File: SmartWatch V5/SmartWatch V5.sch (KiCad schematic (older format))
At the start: 65 parts, among them J1 10118192-0001LF, J10 TestPad, J11 TestPad, J12 TestPad, J13 TestPad, J14 TestPad, J15 TestPad, J16 TestPad, J17 TestPad, J18 TestPad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

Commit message: Switched LCD_EN with LCD_CS so LCD can remain active using RTC pullup
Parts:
- removed J11, J12, J13, J14: TestPad, CustomFootprints:TESTPAD, symbol CustomParts:TestPad
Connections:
- net LCD_CS: now also U6.27 (IO16); no longer U6.13 (IO14)
- net LCD_LED: now also U6.13 (IO14); no longer U6.27 (IO16)
- no-connect marks 19 -> 23
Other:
- moved on the sheet: C1, C11, R23, U1
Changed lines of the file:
@@
 IO15
-$Comp
-L CustomParts:TestPad J12
-U 1 1 5F244C41
-P 3950 6700
-F 0 "J12" H 4178 6751 50  0000 L CNN
-F 1 "TestPad" H 4178 6660 50  0000 L CNN
-F 2 "CustomFootprints:TESTPAD" H 4050 6800 50  0001 C CNN
-F 3 "" H 4050 6800 50  0001 C CNN
-	1    3950 6700
-	1    0    0    -1
-$EndComp
-$Comp
-L CustomParts:TestPad J11
-U 1 1 5F244C47
-P 3950 6500
-F 0 "J11" H 4178 6551 50  0000 L CNN
-F 1 "TestPad" H 4178 6460 50  0000 L CNN
-F 2 "CustomFootprints:TESTPAD" H 4050 6600 50  0001 C CNN
-F 3 "" H 4050 6600 50  0001 C CNN
-	1    3950 6500
-	1    0    0    -1
-$EndComp
-$Comp
-L CustomParts:TestPad J14
-U 1 1 5F2B6D2C
-P 3950 7100
-F 0 "J14" H 4178 7151 50  0000 L CNN
-F 1 "TestPad" H 4178 7060 50  0000 L CNN
-F 2 "CustomFootprints:TESTPAD" H 4050 7200 50  0001 C CNN
-F 3 "" H 4050 7200 50  0001 C CNN
-	1    3950 7100
-	1    0    0    -1
-$EndComp
-$Comp
-L CustomParts:TestPad J13
-U 1 1 5F2B6D32
-P 3950 6900
-F 0 "J13" H 4178 6951 50  0000 L CNN
-F 1 "TestPad" H 4178 6860 50  0000 L CNN
-F 2 "CustomFootprints:TESTPAD" H 4050 7000 50  0001 C CNN
-F 3 "" H 4050 7000 50  0001 C CNN
-	1    3950 6900
-	1    0    0    -1
-$EndComp
-Wire Wire Line
-	3800 6500 3950 6500
-Wire Wire Line
-	3800 6600 3950 6600
-Wire Wire Line
-	3950 6600 3950 6700
-Wire Wire Line
-	3800 6700 3900 6700
-Wire Wire Line
-	3900 6700 3900 6900
-Wire Wire Line
-	3900 6900 3950 6900
-Wire Wire Line
-	3800 6800 3850 6800
-Wire Wire Line
-	3850 6800 3850 7100
-Wire Wire Line
-	3850 7100 3950 7100
 $Comp
 L CustomParts:TSC2003IPWR U10
@@
 	10100 2450 10300 2450
 Wire Wire Line
+	8050 2550 7600 2550
+Wire Wire Line
+	8050 2750 7600 2750
+Wire Wire Line
+	8050 2950 7600 2950
+Wire Wire Line
+	8050 3150 7600 3150
+Wire Wire Line
 	8050 2350 7600 2350
-Wire Wire Line
-	8050 2750 7600 2750
-Wire Wire Line
-	8050 2950 7600 2950
-Wire Wire Line
-	8050 3150 7600 3150
-Wire Wire Line
-	8050 2550 7600 2550
-Text Label 8050 2350 2    50   ~ 0
+Text Label 8050 2550 2    50   ~ 0
 LCD_CS
 Text Label 8050 2750 2    50   ~ 0
@@
 Text Label 8050 3150 2    50   ~ 0
 LCD_MOSI
-Text Label 8050 2550 2    50   ~ 0
+Text Label 8050 2350 2    50   ~ 0
 LCD_LED
 Text Label 8050 3050 2    50   ~ 0
@@
 Wire Wire Line
 	2250 2550 2350 2550
-Text Label 2250 4100 0    50   ~ 0
+Text Label 2300 3900 0    50   ~ 0
 MAX_REG
 $Comp
 L power:GND #PWR0142
 U 1 1 5EB73B93
-P 1400 4000
-F 0 "#PWR0142" H 1400 3750 50  0001 C CNN
-F 1 "GND" H 1405 3827 50  0000 C CNN
-F 2 "" H 1400 4000 50  0001 C CNN
-F 3 "" H 1400 4000 50  0001 C CNN
-	1    1400 4000
+P 1450 3800
+F 0 "#PWR0142" H 1450 3550 50  0001 C CNN
+F 1 "GND" H 1455 3627 50  0000 C CNN
+F 2 "" H 1450 3800 50  0001 C CNN
+F 3 "" H 1450 3800 50  0001 C CNN
+	1    1450 3800
 	1    0    0    -1
 $EndComp
@@
 L power:GND #PWR02
 U 1 1 5EEB600A
-P 2250 4400
-F 0 "#PWR02" H 2250 4150 50  0001 C CNN
-F 1 "GND" H 2255 4227 50  0000 C CNN
-F 2 "" H 2250 4400 50  0001 C CNN
-F 3 "" H 2250 4400 50  0001 C CNN
-	1    2250 4400
-	1    0    0    -1
-$EndComp
-Wire Wire Line
-	2200 4100 2250 4100
+P 2300 4200
+F 0 "#PWR02" H 2300 3950 50  0001 C CNN
+F 1 "GND" H 2305 4027 50  0000 C CNN
+F 2 "" H 2300 4200 50  0001 C CNN
+F 3 "" H 2300 4200 50  0001 C CNN
+	1    2300 4200
+	1    0    0    -1
+$EndComp
+Wire Wire Line
+	2250 3900 2300 3900
 $Comp
 L Device:C C11
 U 1 1 5EE9CCD7
-P 2250 4250
-F 0 "C11" H 2365 4296 50  0000 L CNN
-F 1 "0.1uF" H 2365 4205 50  0000 L CNN
-F 2 "Capacitor_SMD:C_0603_1608Metric" H 2288 4100 50  0001 C CNN
-F 3 "~" H 2250 4250 50  0001 C CNN
-F 4 "1276-1006-1-ND" H 2250 4250 50  0001 C CNN "digikey"
-	1    2250 4250
+P 2300 4050
+F 0 "C11" H 2415 4096 50  0000 L CNN
+F 1 "0.1uF" H 2415 4005 50  0000 L CNN
+F 2 "Capacitor_SMD:C_0603_1608Metric" H 2338 3900 50  0001 C CNN
+F 3 "~" H 2300 4050 50  0001 C CNN
+F 4 "1276-1006-1-ND" H 2300 4050 50  0001 C CNN "digikey"
+	1    2300 4050
 	1    0    0    -1
 $EndComp
@@
 L power:GND #PWR01
 U 1 1 5EE9C540
-P 1800 4250
-F 0 "#PWR01" H 1800 4000 50  0001 C CNN
-F 1 "GND" H 1800 4100 50  0000 C CNN
-F 2 "" H 1800 4250 50  0001 C CNN
-F 3 "" H 1800 4250 50  0001 C CNN
-	1    1800 4250
-	1    0    0    -1
-$EndComp
-Wire Wire Line
-	2200 3950 2650 3950
-Wire Wire Line
-	2200 3850 2650 3850
-Text Label 2650 3950 2    50   ~ 0
+P 1850 4050
+F 0 "#PWR01" H 1850 3800 50  0001 C CNN
+F 1 "GND" H 1850 3900 50  0000 C CNN
+F 2 "" H 1850 4050 50  0001 C CNN
+F 3 "" H 1850 4050 50  0001 C CNN
+	1    1850 4050
+	1    0    0    -1
+$EndComp
+Wire Wire Line
+	2250 3750 2700 3750
+Wire Wire Line
+	2250 3650 2700 3650
+Text Label 2700 3750 2    50   ~ 0
 I2C_SCL
-Text Label 2650 3850 2    50   ~ 0
+Text Label 2700 3650 2    50   ~ 0
 I2C_SDA
 Wire Wire Line
-	2200 3750 2650 3750
-Text Label 2650 3750 2    50   ~ 0
+	2250 3550 2700 3550
+Text Label 2700 3550 2    50   ~ 0
 BAT_ALRT
 Wire Wire Line
-	2050 3300 2650 3300
-Text Label 2650 3300 2    50   ~ 0
+	2100 3100 2700 3100
+Text Label 2700 3100 2    50   ~ 0
 BAT_SENSE
-Connection ~ 2050 3300
-Wire Wire Line
-	2050 3300 2050 3350
-Wire Wire Line
-	1950 3300 2050 3300
-Connection ~ 1600 3300
-Wire Wire Line
-	900  3300 900  3800
-Wire Wire Line
-	1600 3300 900  3300
-Wire Wire Line
-	1600 3300 1650 3300
-Wire Wire Line
-	1600 3350 1600 3300
+Connection ~ 2100 3100
+Wire Wire Line
+	2100 3100 2100 3150
+Wire Wire Line
+	2000 3100 2100 3100
+Connection ~ 1650 3100
+Wire Wire Line
+	950  3100 950  3600
+Wire Wire Line
+	1650 3100 950  3100
+Wire Wire Line
+	1650 3100 1700 3100
+Wire Wire Line
+	1650 3150 1650 3100
 $Comp
 L Device:R R23
 U 1 1 5EBB9EAC
-P 1800 3300
-F 0 "R23" H 1870 3346 50  0000 L CNN
-F 1 "10m" H 1870 3255 50  0000 L CNN
-F 2 "Resistor_SMD:R_0805_2012Metric" V 1730 3300 50  0001 C CNN
-F 3 "https://d1d2qsbl8m0m72.cloudfront.net/en/products/databook/datasheet/passive/resistor/chip_resistor/pmr-e.pdf" H 1800 3300 50  0001 C CNN
-F 4 "RL12T.010JCT-ND" H 1800 3300 50  0001 C CNN "digikey"
-	1    1800 3300
+P 1850 3100
+F 0 "R23" H 1920 3146 50  0000 L CNN
+F 1 "10m" H 1920 3055 50  0000 L CNN
+F 2 "Resistor_SMD:R_0805_2012Metric" V 1780 3100 50  0001 C CNN
+F 3 "https://d1d2qsbl8m0m72.cloudfront.net/en/products/databook/datasheet/passive/resistor/chip_resistor/pmr-e.pdf" H 1850 3100 50  0001 C CNN
+F 4 "RL12T.010JCT-ND" H 1850 3100 50  0001 C CNN "digikey"
+	1    1850 3100
 	0    -1   -1   0
 $EndComp
 Wire Wire Line
-	1350 3800 1400 3800
-Connection ~ 1350 3800
-Wire Wire Line
-	1350 3900 1350 3800
-Wire Wire Line
-	1400 3900 1350 3900
-Wire Wire Line
-	900  3800 1350 3800
+	1400 3600 1450 3600
+Connection ~ 1400 3600
+Wire Wire Line
+	1400 3700 1400 3600
+Wire Wire Line
+	1450 3700 1400 3700
+Wire Wire Line
+	950  3600 1400 3600
 $Comp
 L Device:C C1
 U 1 1 5E856FED
-P 900 3950
-F 0 "C1" H 600 4000 50  0000 L CNN
-F 1 "10uF" H 600 3900 50  0000 L CNN
-F 2 "Capacitor_SMD:C_0603_1608Metric" H 938 3800 50  0001 C CNN
-F 3 "~" H 900 3950 50  0001 C CNN
-F 4 "478-10766-1-ND" H 900 3950 50  0001 C CNN "digikey"
-	1    900  3950
-	1    0    0    -1
-$EndComp
-Text Label 700  3800 0    50   ~ 0
+P 950 3750
+F 0 "C1" H 650 3800 50  0000 L CNN
+F 1 "10uF" H 650 3700 50  0000 L CNN
+F 2 "Capacitor_SMD:C_0603_1608Metric" H 988 3600 50  0001 C CNN
+F 3 "~" H 950 3750 50  0001 C CNN
+F 4 "478-10766-1-ND" H 950 3750 50  0001 C CNN "digikey"
+	1    950  3750
+	1    0    0    -1
+$EndComp
+Text Label 750  3600 0    50   ~ 0
 BAT+
 Wire Wire Line
-	700  3800 900  3800
-Connection ~ 900  3800
+	750  3600 950  3600
+Connection ~ 950  3600
 $Comp
 L power:GND #PWR0143
 U 1 1 5E91C7C2
-P 900 4100
-F 0 "#PWR0143" H 900 3850 50  0001 C CNN
-F 1 "GND" H 905 3927 50  0000 C CNN
-F 2 "" H 900 4100 50  0001 C CNN
-F 3 "" H 900 4100 50  0001 C CNN
-	1    900  4100
+P 950 3900
+F 0 "#PWR0143" H 950 3650 50  0001 C CNN
+F 1 "GND" H 955 3727 50  0000 C CNN
+F 2 "" H 950 3900 50  0001 C CNN
+F 3 "" H 950 3900 50  0001 C CNN
+	1    950  3900
 	1    0    0    -1
 $EndComp
@@
 L CustomParts:MAX17260 U1
 U 1 1 5F23D031
-P 1800 3850
-F 0 "U1" H 1250 4550 50  0000 C CNN
-F 1 "MAX17260" H 1400 4450 50  0000 C CNN
-F 2 "CustomFootprints:TDFN16-EP" H 1150 5000 50  0001 C CNN
-F 3 "https://datasheets.maximintegrated.com/en/ds/MAX17260.pdf" H 1150 5000 50  0001 C CNN
-F 4 "175-MAX17260SEWL+TCT-ND" H 850 4900 50  0001 C CNN "digikey"
-	1    1800 3850
+P 1850 3650
+F 0 "U1" H 1300 4350 50  0000 C CNN
+F 1 "MAX17260" H 1450 4250 50  0000 C CNN
+F 2 "CustomFootprints:TDFN16-EP" H 1200 4800 50  0001 C CNN
+F 3 "https://datasheets.maximintegrated.com/en/ds/MAX17260.pdf" H 1200 4800 50  0001 C CNN
+F 4 "175-MAX17260SEWL+TCT-ND" H 900 4700 50  0001 C CNN "digikey"
+	1    1850 3650
 	1    0    0    -1
 $EndComp
@@
 Wire Bus Line
 	3150 3250 5900 3250
-Text Notes 3500 2950 0    50   ~ 0
+Text Notes 3500 3000 0    50   ~ 0
 Charging Current of 100mA\n
 Wire Bus Line
@@
 Wire Bus Line
 	6050 5950 6050 6500
+NoConn ~ 3800 6500
+NoConn ~ 3800 6600
+NoConn ~ 3800 6700
+NoConn ~ 3800 6800
 $EndSCHEMATC

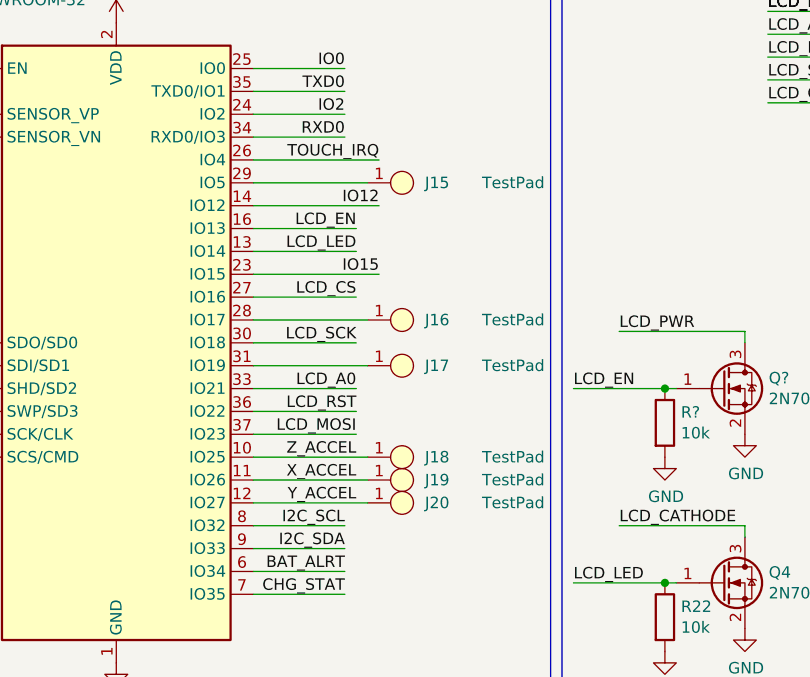
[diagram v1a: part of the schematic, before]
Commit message: Removed testpads that are no longer needed
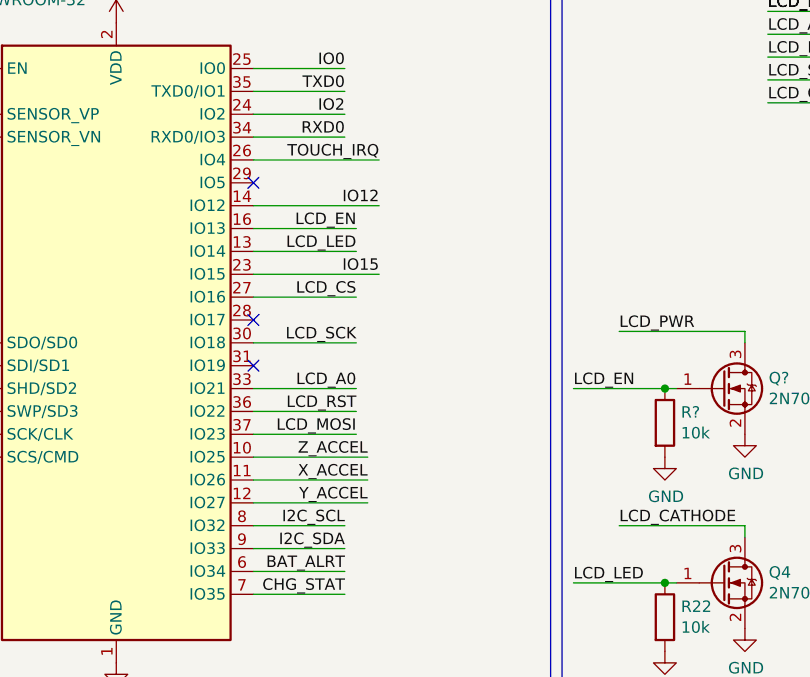
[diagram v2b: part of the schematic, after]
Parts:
- removed J15, J16, J17, J18, J19, J20: TestPad, CustomFootprints:TESTPAD, symbol CustomParts:TestPad
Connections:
- no-connect marks 23 -> 26
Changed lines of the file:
@@
 Text Label 9850 1700 0    50   ~ 0
 LCD_CS
-$Comp
-L CustomParts:TestPad J15
-U 1 1 5F1F3B31
-P 8100 2050
-F 0 "J15" H 8350 2050 50  0000 L CNN
-F 1 "TestPad" H 8600 2050 50  0000 L CNN
-F 2 "CustomFootprints:TESTPAD" H 8200 2150 50  0001 C CNN
-F 3 "" H 8200 2150 50  0001 C CNN
-	1    8100 2050
-	1    0    0    -1
-$EndComp
-$Comp
-L CustomParts:TestPad J16
-U 1 1 5F1F47AF
-P 8100 2650
-F 0 "J16" H 8350 2650 50  0000 L CNN
-F 1 "TestPad" H 8600 2650 50  0000 L CNN
-F 2 "CustomFootprints:TESTPAD" H 8200 2750 50  0001 C CNN
-F 3 "" H 8200 2750 50  0001 C CNN
-	1    8100 2650
-	1    0    0    -1
-$EndComp
-$Comp
-L CustomParts:TestPad J17
-U 1 1 5F1F4D94
-P 8100 2850
-F 0 "J17" H 8350 2850 50  0000 L CNN
-F 1 "TestPad" H 8600 2850 50  0000 L CNN
-F 2 "CustomFootprints:TESTPAD" H 8200 2950 50  0001 C CNN
-F 3 "" H 8200 2950 50  0001 C CNN
-	1    8100 2850
-	1    0    0    -1
-$EndComp
-$Comp
-L CustomParts:TestPad J18
-U 1 1 5F1F51C0
-P 8100 3250
-F 0 "J18" H 8350 3250 50  0000 L CNN
-F 1 "TestPad" H 8600 3250 50  0000 L CNN
-F 2 "CustomFootprints:TESTPAD" H 8200 3350 50  0001 C CNN
-F 3 "" H 8200 3350 50  0001 C CNN
-	1    8100 3250
-	1    0    0    -1
-$EndComp
-$Comp
-L CustomParts:TestPad J19
-U 1 1 5F1F5439
-P 8100 3350
-F 0 "J19" H 8350 3350 50  0000 L CNN
-F 1 "TestPad" H 8600 3350 50  0000 L CNN
-F 2 "CustomFootprints:TESTPAD" H 8200 3450 50  0001 C CNN
-F 3 "" H 8200 3450 50  0001 C CNN
-	1    8100 3350
-	1    0    0    -1
-$EndComp
-$Comp
-L CustomParts:TestPad J20
-U 1 1 5F1F569A
-P 8100 3450
-F 0 "J20" H 8350 3450 50  0000 L CNN
-F 1 "TestPad" H 8600 3450 50  0000 L CNN
-F 2 "CustomFootprints:TESTPAD" H 8200 3550 50  0001 C CNN
-F 3 "" H 8200 3550 50  0001 C CNN
-	1    8100 3450
-	1    0    0    -1
-$EndComp
-Wire Wire Line
-	7600 2050 8100 2050
-Wire Wire Line
-	7600 2650 8100 2650
-Wire Wire Line
-	7600 2850 8100 2850
 Wire Wire Line
 	7600 3250 8100 3250
@@
 Wire Bus Line
 	5900 4650 5900 3300
-Text Label 8050 3250 2    50   ~ 0
+Text Label 8100 3250 2    50   ~ 0
 Z_ACCEL
-Text Label 8050 3350 2    50   ~ 0
+Text Label 8100 3350 2    50   ~ 0
 X_ACCEL
-Text Label 8050 3450 2    50   ~ 0
+Text Label 8100 3450 2    50   ~ 0
 Y_ACCEL
 Text Label 4200 2350 2    50   ~ 0
@@
 NoConn ~ 3800 6700
 NoConn ~ 3800 6800
+NoConn ~ 7600 2050
+NoConn ~ 7600 2650
+NoConn ~ 7600 2850
 $EndSCHEMATC

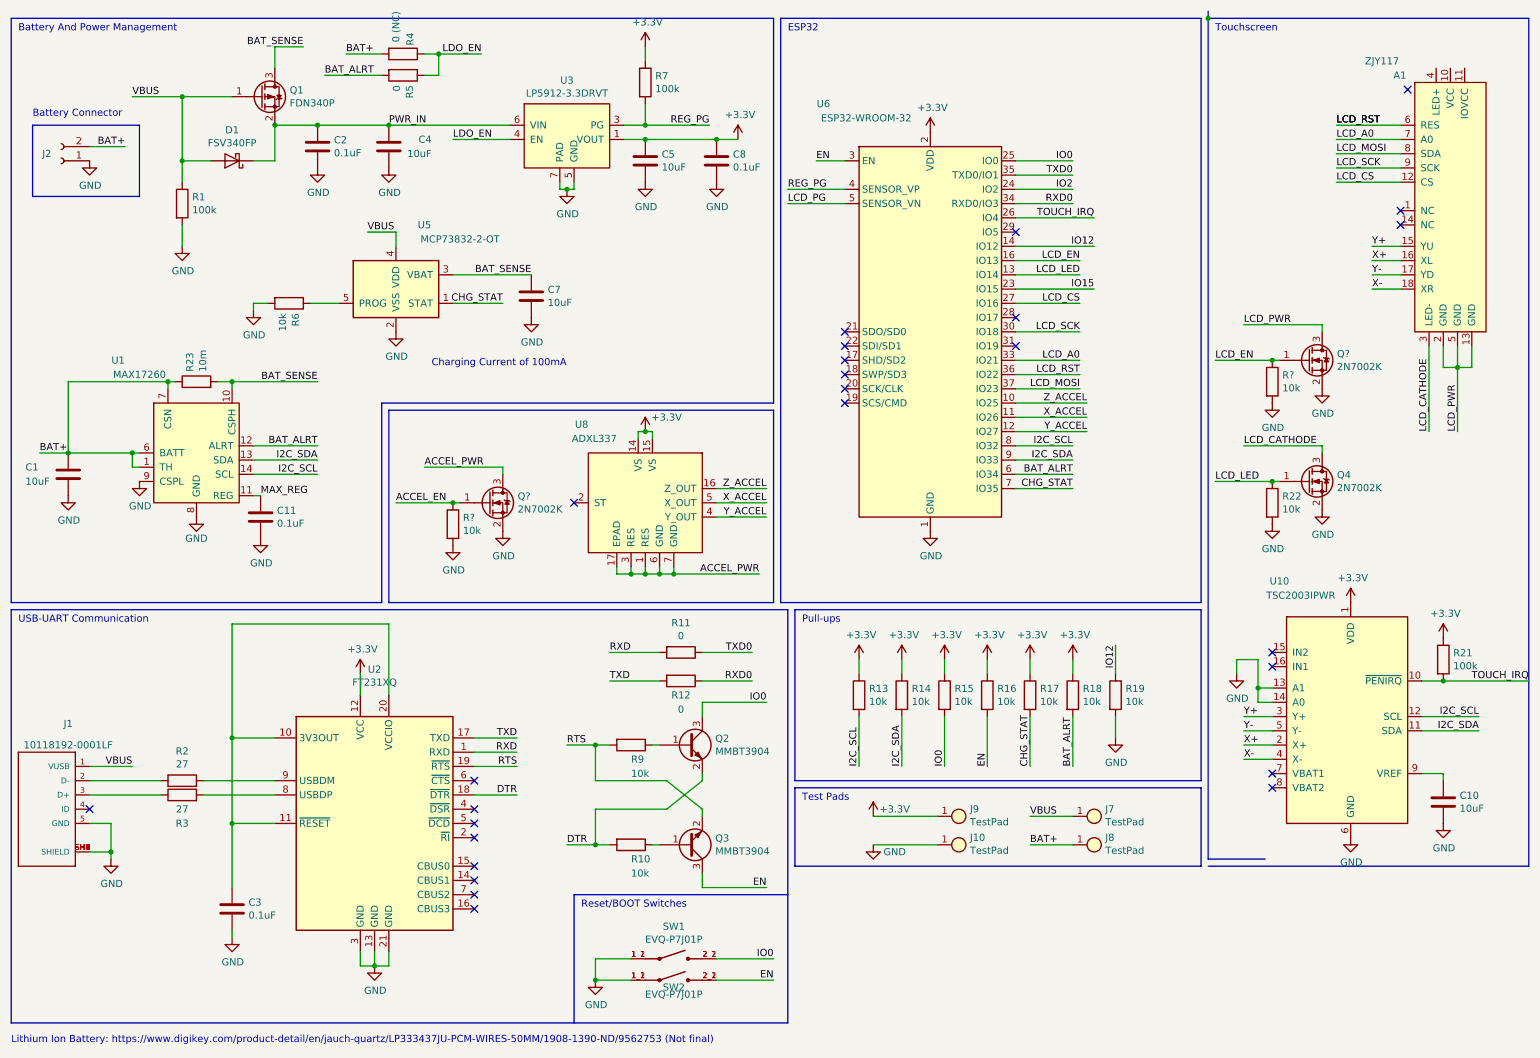
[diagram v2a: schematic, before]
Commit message: Added Optional Thermistor for battery monitor
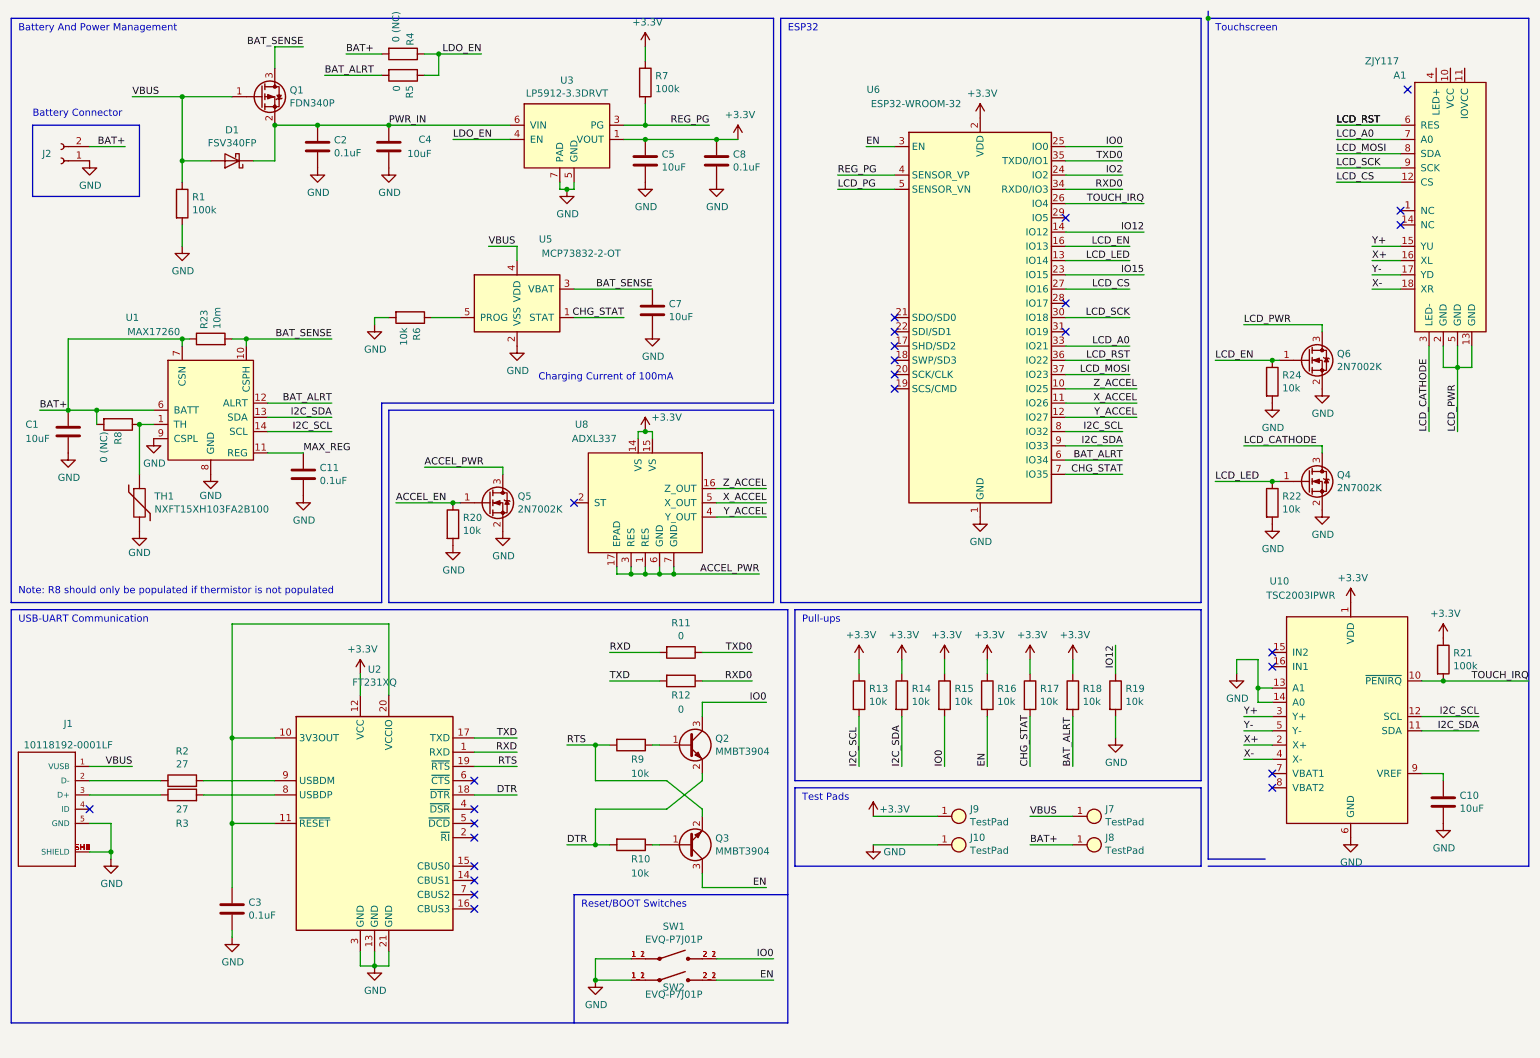
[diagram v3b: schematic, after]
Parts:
- added R8: 0 (NC), Resistor_SMD:R_0603_1608Metric, symbol Device:R
- added TH1: NXFT15XH103FA2B100, symbol Device:Thermistor
- gave numbers to parts that had none: 4
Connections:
- net BAT+: now also R8.2; no longer U1.1 (TH)
- net GND: now also TH1.2
- new net: R8.1, TH1.1, U1.1 (TH)
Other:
- note added: "Note: R8 should only be populated if thermistor is not populated"
- note removed: "Lithium Ion Battery: https://www.digikey.com/product-detail/en/jauch-quartz/LP333437JU-PCM-WIRES-50MM/1908-1390-ND/9562753 (Not final)\n"
- moved on the sheet: C1, C11, C7, R23, R6, U1, U5, U6
